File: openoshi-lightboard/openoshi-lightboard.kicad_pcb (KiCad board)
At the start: 2 copper layers, 30 x 30 mm, 29 parts, among them J1 USB_C_Receptacle_PowerOnly_6P, Q1 PMZ600UNE, Q2 PMZ600UNE, Q3 PMZ600UNE, Q4 PMZ600UNE, SW1 AKE31A, SW2 AKE31A, U1 CH32V003FxUx, U2 TLV61070A, U3 MCP73831-2-OT

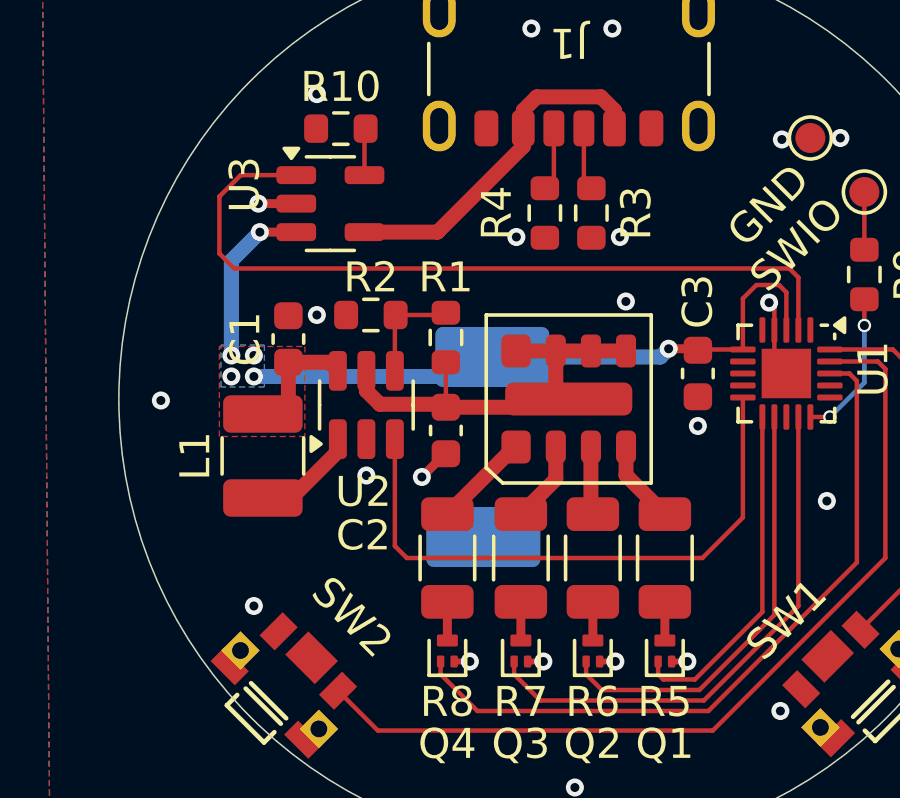
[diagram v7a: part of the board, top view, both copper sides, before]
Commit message: Assembly files created, first run
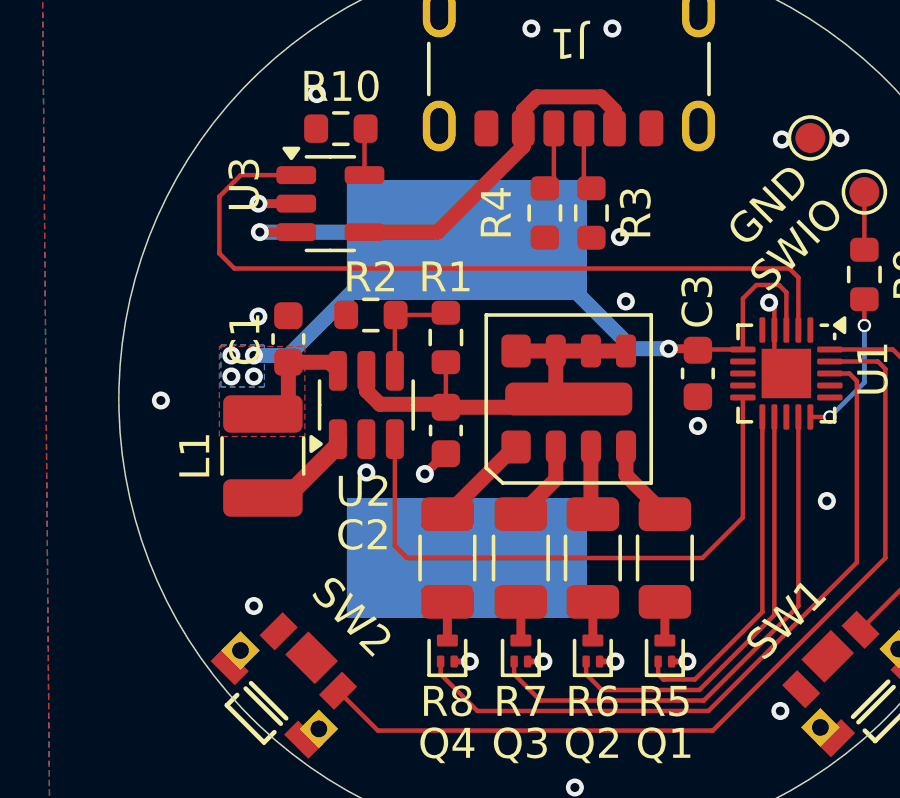
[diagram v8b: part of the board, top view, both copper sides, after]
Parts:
- TP3, TP4: footprint TestPoint:TestPoint_Keystone_5019_Miniature -> openoshi-lightboard:Battery_SolderPad
- moved TP3 3.99 mm to (146.6, 94.7)
- moved TP4 0.89 mm to (146.6, 105.3)
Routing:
- net +BATT: track 30.4 -> 35.6 mm
- net GND: track 7.12 -> 6.98 mm, vias 24 -> 23
